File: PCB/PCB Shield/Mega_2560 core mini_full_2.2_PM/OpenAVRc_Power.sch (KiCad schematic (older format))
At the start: 24 parts, among them P17 BATT, P21 Sw_power, P26 LCD_Alim, P30 MiniDCDC3A, Q3 MMBT2222ALT1, Q4 SI2319DS, U4 PM5033, U5 LD1117S33TR

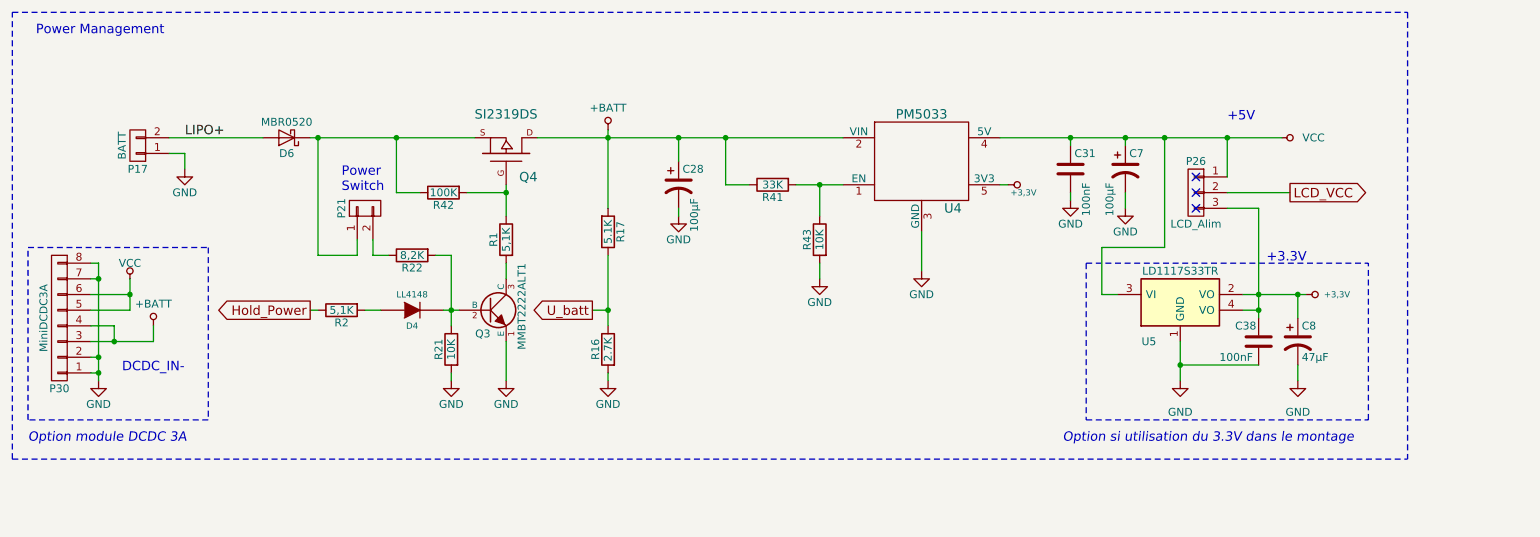
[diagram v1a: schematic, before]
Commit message: Update PCB files V2.2
Move r5 after r6
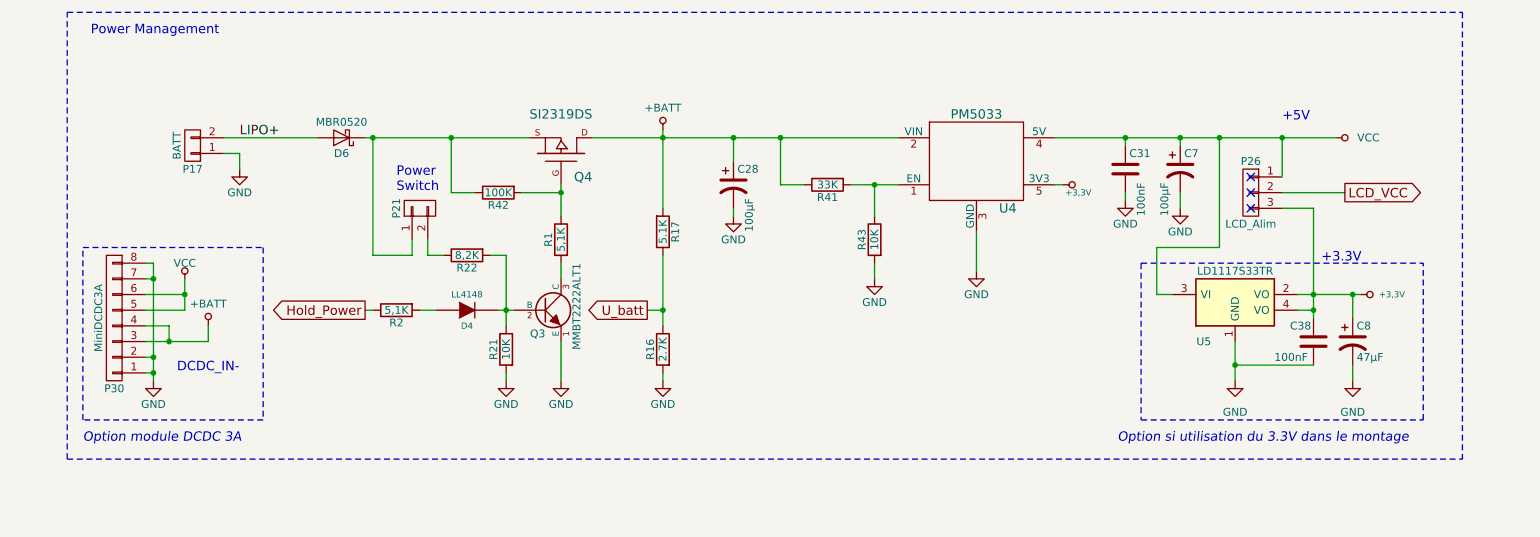
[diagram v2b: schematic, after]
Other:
- moved on the sheet: C28, C31, C38, C7, C8, D4, D6, P17, P21, P26, P30, Q3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

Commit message: Add bitmaps in schematics files for fun.
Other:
- note added: "Option module DCDC 3A\n MP1584EN"
- note added: "Options:\n1 - MP1584EN (+5V) (câbler U5 si besoin +3,3v) (U4 non câblé)\n2 - PM5033 (+5v et +3,3) (MP1584EN et U5 non câblés)"
- note removed: "Option module DCDC 3A"
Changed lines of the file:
@@
 Sheet 7 7
 Title "Shield Mega2560 core Full"
-Date "2019-09-02"
+Date "2019-09-14"
 Rev "2.2"
 Comp "© Team OpenAVRc"
@@
 	1    0    0    -1
 $EndComp
-Text Notes 1950 4950 0    60   Italic 0
-Option module DCDC 3A
+Text Notes 1950 5000 0    60   Italic 0
+Option module DCDC 3A\n       MP1584EN
 $Comp
 L power1:+BATT #PWR0119
@@
 EndData
 $EndBitmap
+Text Notes 1950 5450 0    60   ~ 0
+Options:\n1 - MP1584EN (+5V) (câbler U5 si besoin +3,3v) (U4 non câblé)\n2 - PM5033 (+5v et +3,3) (MP1584EN et U5 non câblés)
 $EndSCHEMATC
